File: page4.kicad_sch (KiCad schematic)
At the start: 83 parts, among them U25 TL082, U26 TL084

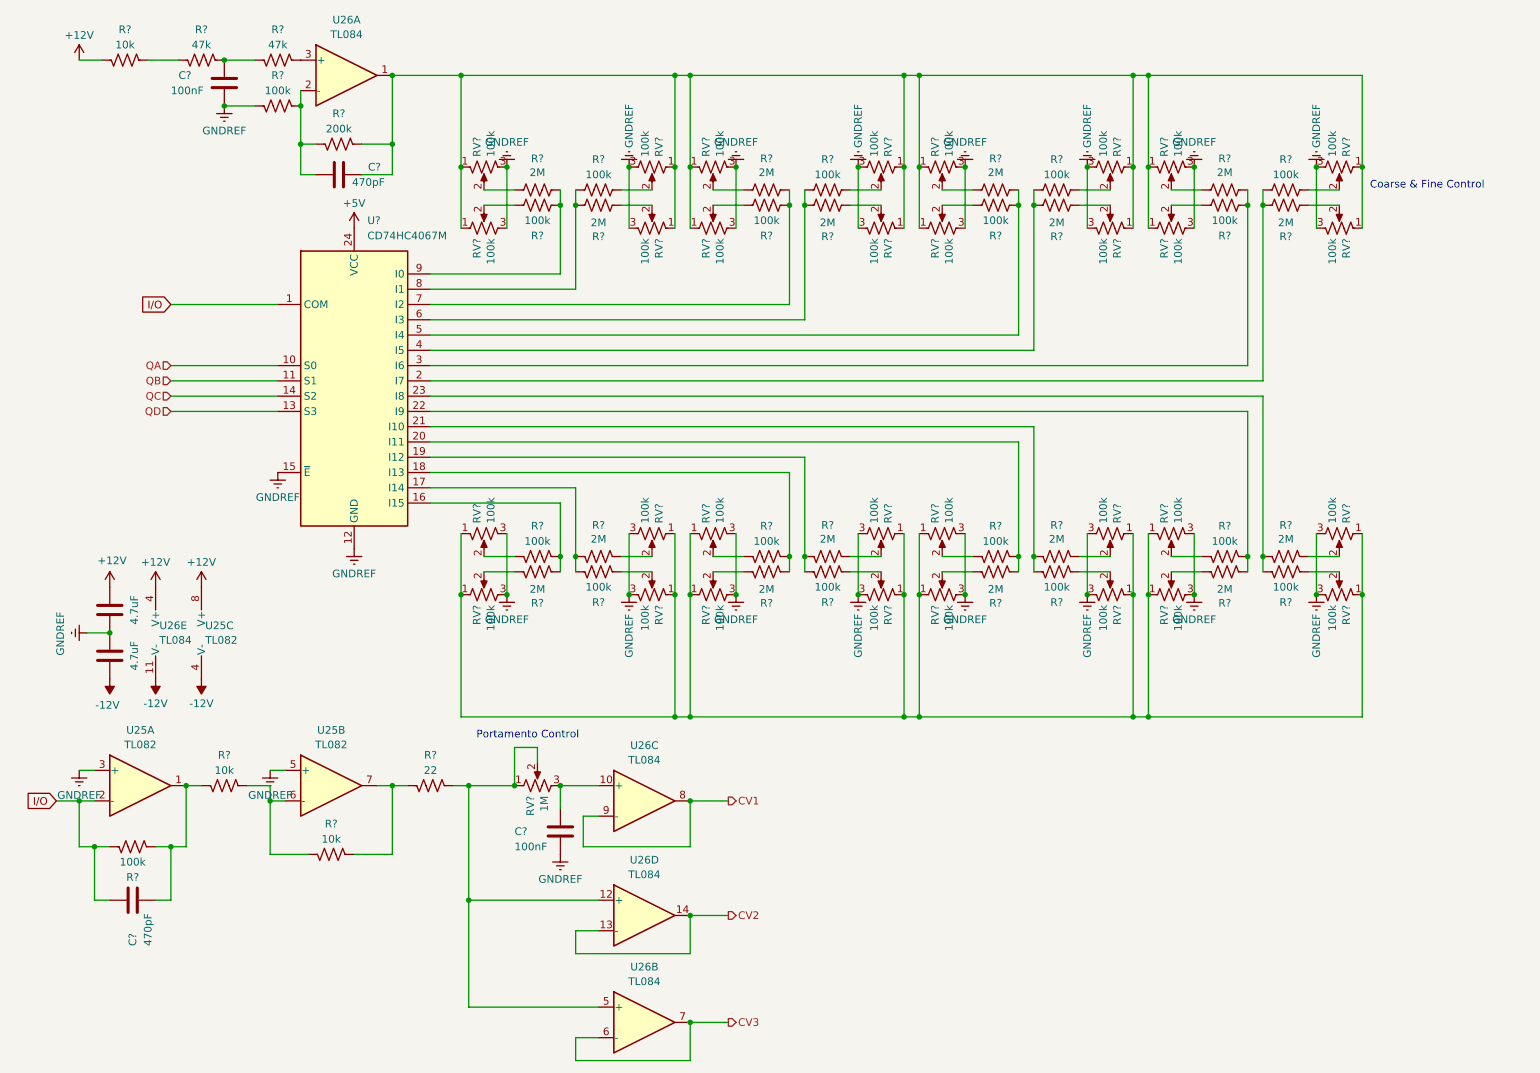
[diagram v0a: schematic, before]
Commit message: created pcb file, placed parts
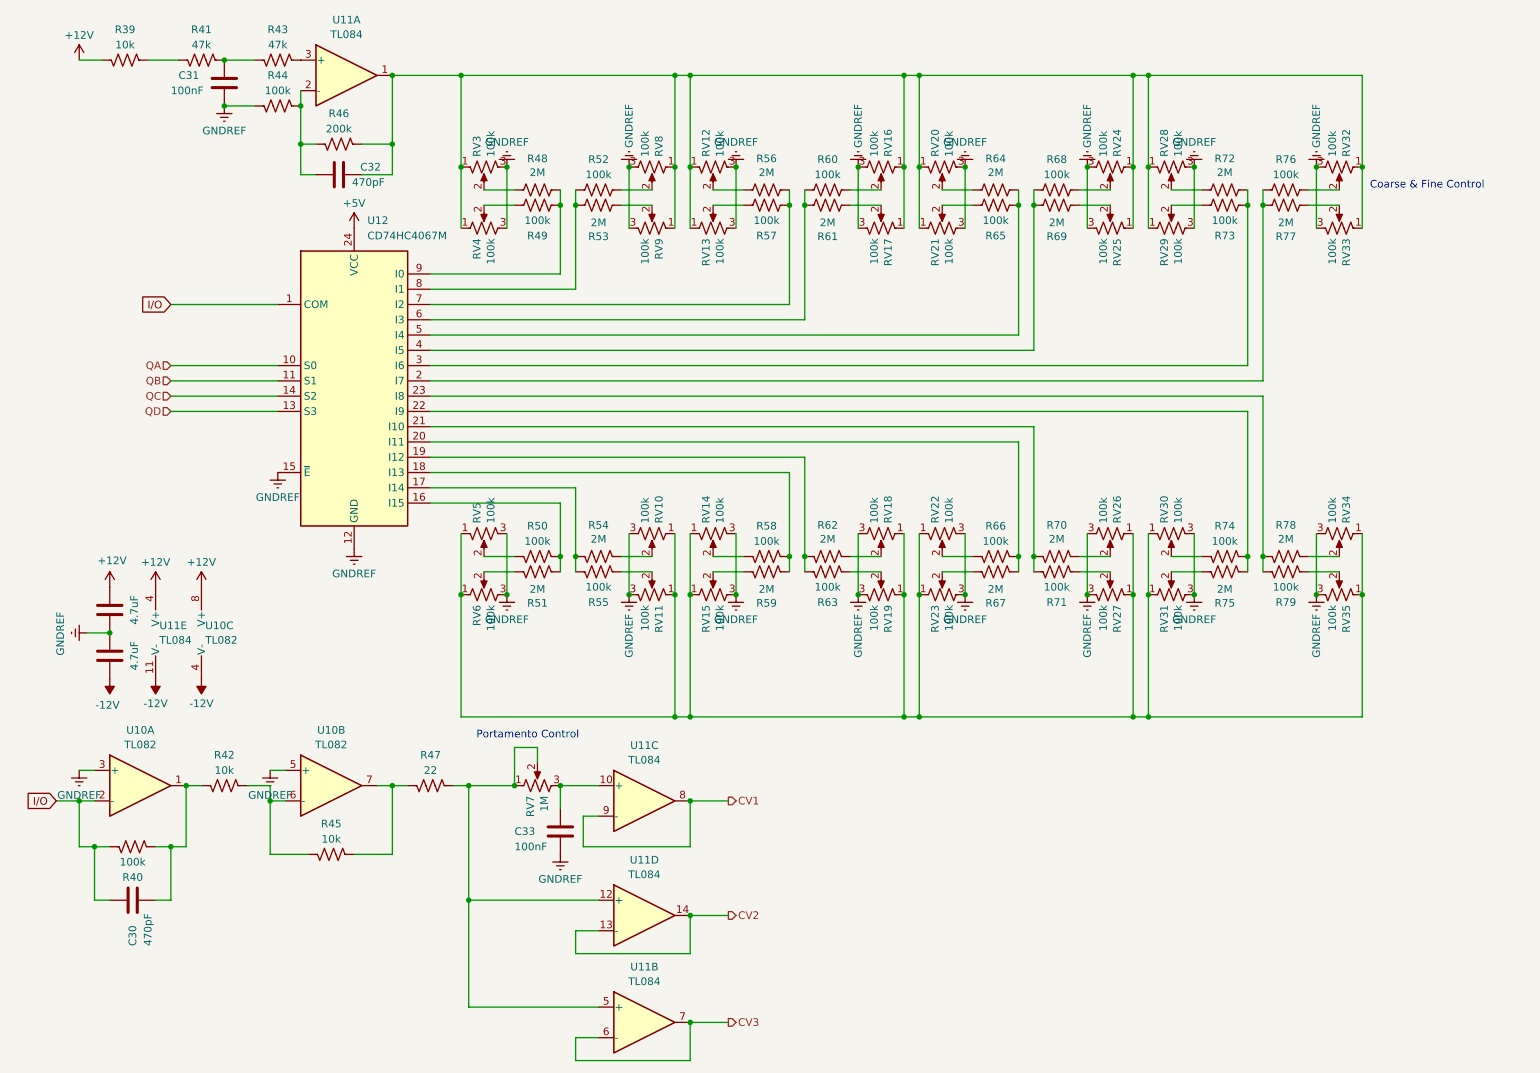
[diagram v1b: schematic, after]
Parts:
- gave numbers to parts that had none: 81
- renumbered U25 to U10, U26 to U11

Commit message: init placement/layout
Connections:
- net at RV22.2: now also R67.1; no longer R66.2
- net at R60.1, U12.6 (I3): now also R61.2; no longer R61.1
- net at RV16.2: now also R61.1; no longer R60.2
- net at R76.1, U12.2 (I7): now also R77.2; no longer R77.1
- net at R68.1, U12.4 (I5): now also R69.2; no longer R69.1
- net at R52.1, U12.8 (I1): now also R53.2; no longer R53.1
- net at R59.2: now also R58.2, U12.18 (I13); no longer RV15.2
- net at RV9.2: now also R52.2; no longer R53.2
- net at R75.2: now also R74.2, U12.22 (I9); no longer RV31.2
- net at RV33.2: now also R76.2; no longer R77.2
- net at R51.2: now also R50.2, U12.16 (I15); no longer RV6.2
- net at RV24.2: now also R69.1; no longer R68.2
- net at RV25.2: now also R68.2; no longer R69.2
- net at RV5.2: now also R51.1; no longer R50.2
- net at RV32.2: now also R77.1; no longer R76.2
- net at RV14.2: now also R59.1; no longer R58.2
- net at RV30.2: now also R75.1; no longer R74.2
- net at RV8.2: now also R53.1; no longer R52.2
- net at R67.2: now also R66.2, U12.20 (I11); no longer RV23.2
- net at RV17.2: now also R60.2; no longer R61.2
- new net: R50.1, RV6.2
- new net: R58.1, RV15.2
- new net: R74.1, RV31.2
- new net: R66.1, RV23.2

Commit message: routed 100%
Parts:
- removed C28, C29: 4.7uF, Capacitor_SMD:C_0805_2012Metric, symbol Device:C
- added C50, C52 (x3): 470nF, Capacitor_SMD:C_0805_2012Metric, symbol Device:C
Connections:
- net +12V: now also C52.1, C52.1
- net -12V: now also C50.2, C52.2
- net GNDREF: now also C50.1, C52.1, C52.2, C52.2

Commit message: lots of work... created faceplate
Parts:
- C33: value 100nF -> 1uF
- R48, R51, R53, R54, R56, R59, R61, R62, R64, R67, R69, R70, R72, R75, R77, R78: value 2M -> 1M
- R49, R50, R52, R55, R57, R58, R60, R63, R65, R66, R68, R71, R73, R74, R76, R79, RV10, RV11, RV12, RV13, RV14, RV15, RV16, RV17, RV18, RV19, RV20, RV21, RV22, RV23, RV24, RV25, RV26, RV27, RV28, RV29, RV3, RV30, RV31, RV32, RV33, RV34, RV35, RV4, RV5, RV6, RV8, RV9: value 100k -> 50k
- RV7: value 1M -> 50k
